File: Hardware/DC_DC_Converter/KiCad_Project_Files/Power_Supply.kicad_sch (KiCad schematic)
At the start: 104 parts, among them J2 Conn_01x01, J3 Conn_01x01, J4 Screw_Terminal_01x02, J5 USB_C_Receptacle_USB2.0, Q1 FDN335N, Q2 FDN335N, Q3 FDN335N, SW1 UP, SW2 DW, SW3 V_I_SEL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

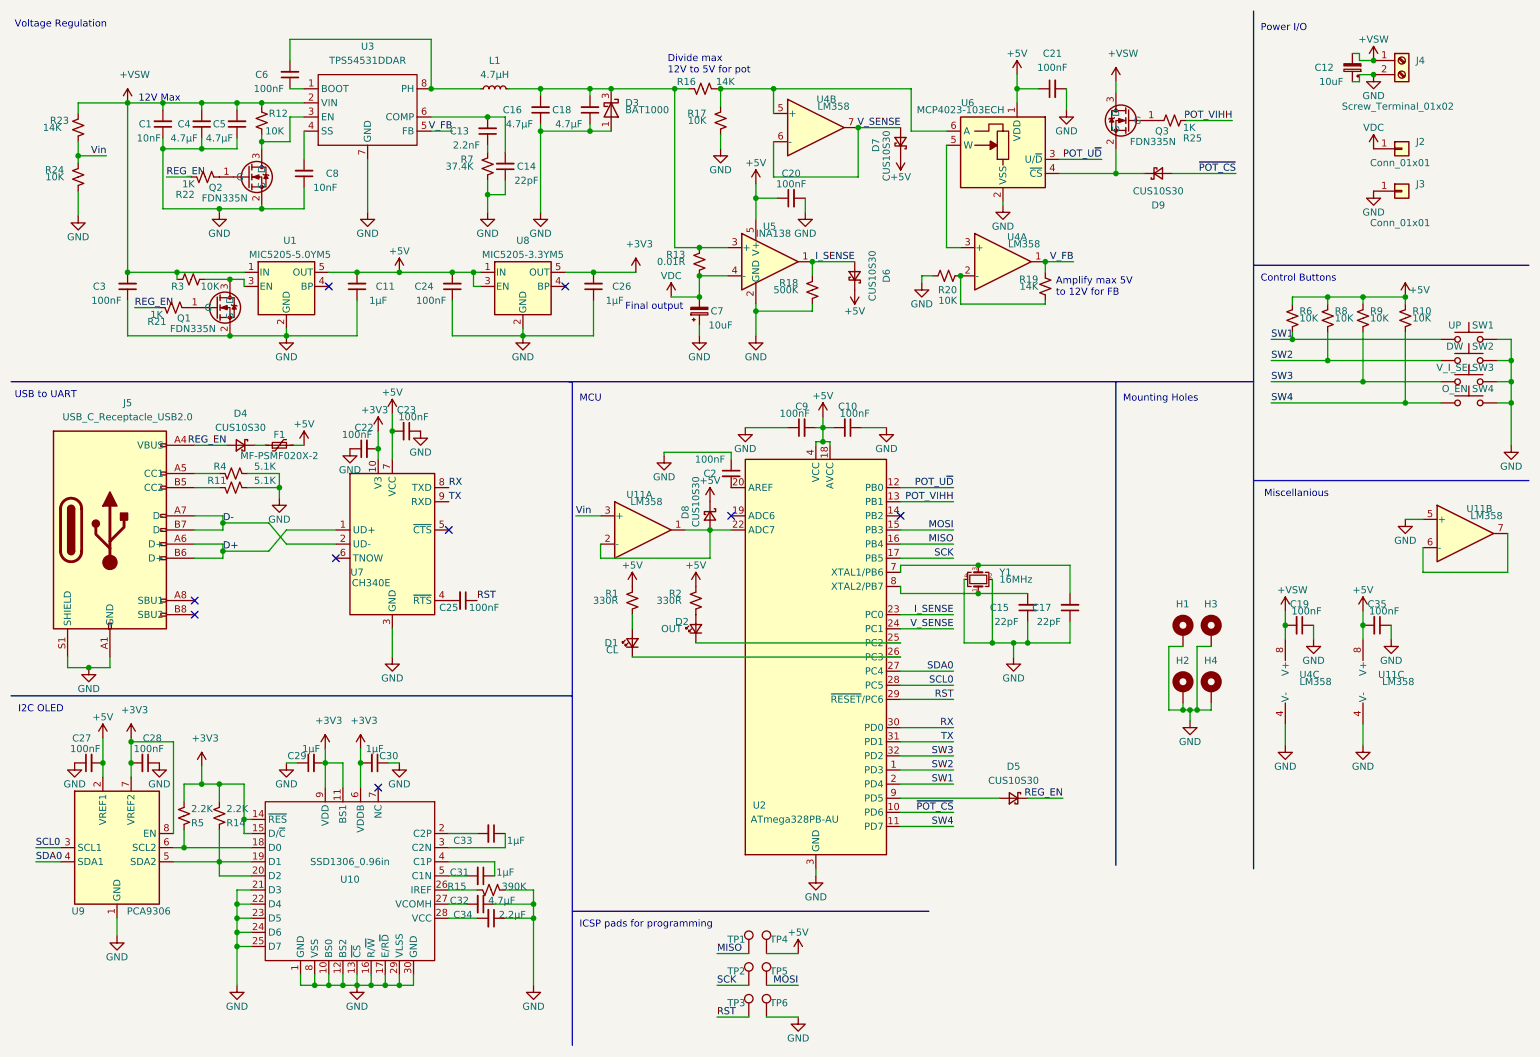
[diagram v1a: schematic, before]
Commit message: fixed buffer errors
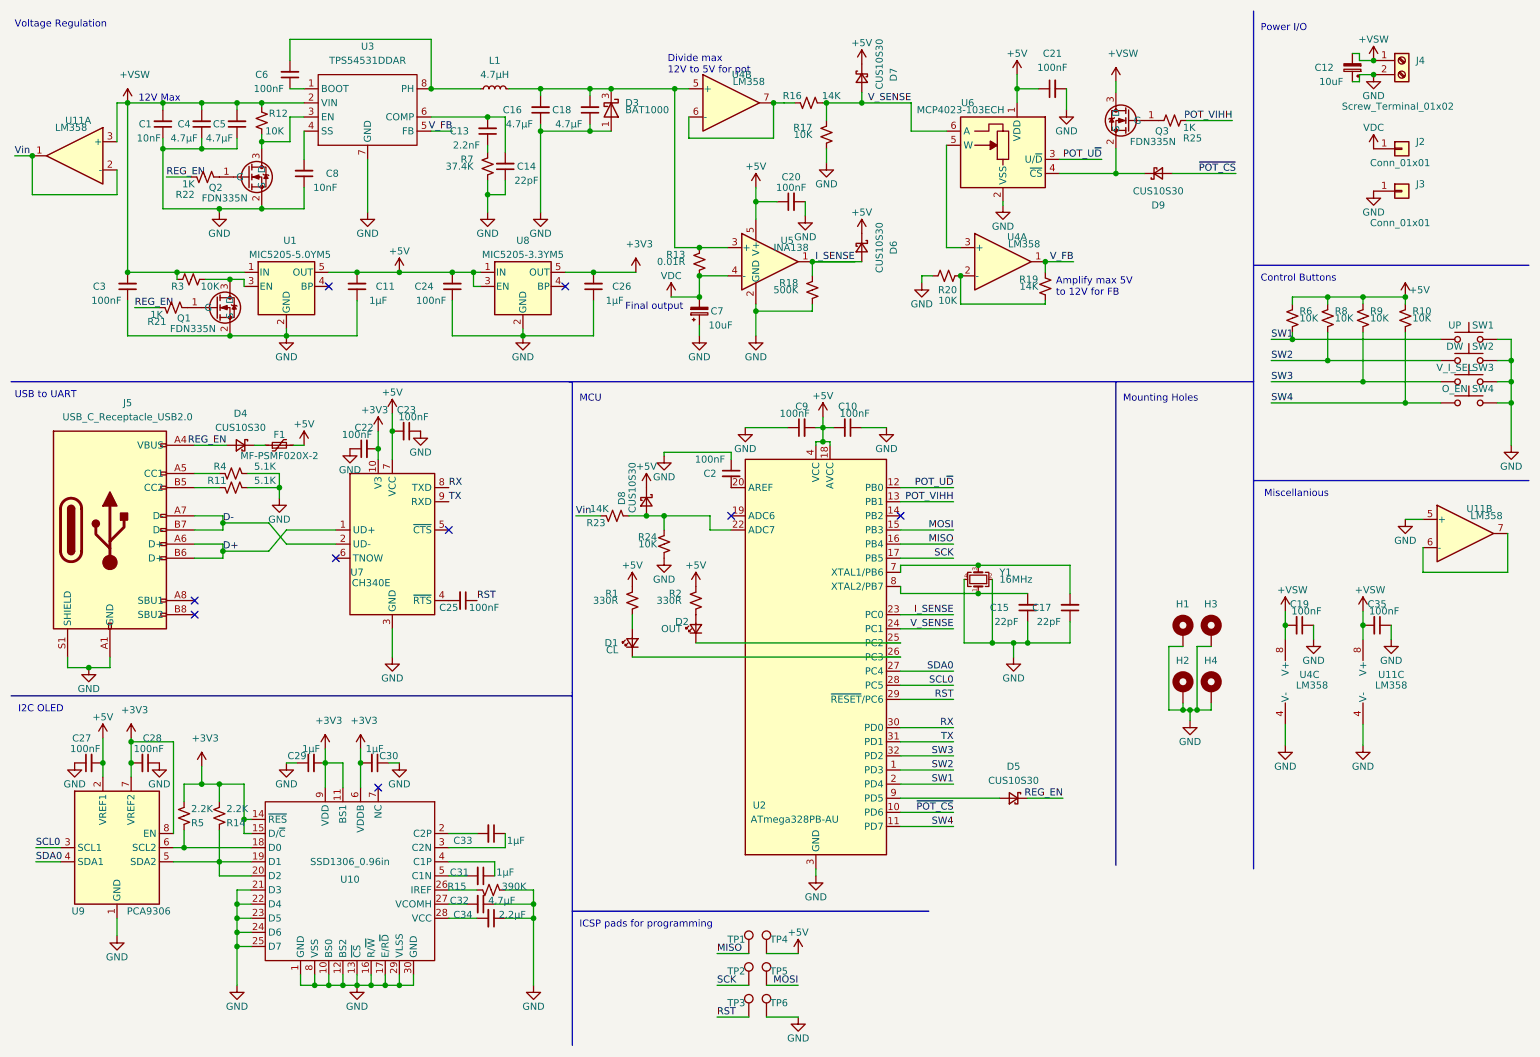
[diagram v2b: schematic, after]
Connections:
- net +5V: no longer C35.2, U11.8 (V+)
- net +VSW: now also C35.2, U11.3 (+), U11.8 (V+); no longer R23.1
- net V_SENSE: now also R16.1, R17.2, U6.6 (A); no longer U4.6 (-), U4.7
- net Vin: now also R23.1, U11.1, U11.2 (-); no longer R23.2, R24.2, U11.3 (+)
- net at C16.2, C18.2, D3.3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: now also U4.5 (+); no longer R16.2
- net at D8.2 (A), U2.22 (ADC7): now also R23.2, R24.2; no longer U11.1, U11.2 (-)
- new net: R16.2, U4.6 (-), U4.7
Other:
- moved on the sheet: C20, D6, D7, D8, R16, R17, R23, R24, U11A, U4B
